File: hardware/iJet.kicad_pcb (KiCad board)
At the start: 2 copper layers, 82.3 x 116.7 mm, 107 parts, among them J1 GPIO, J12 Battery_Meas, J13 ICSP_Header_2, J14 5V_In, J15 Stat_LED, J16 ICSP_Header_1, J17 Button_Header, J18 RPI_POWER, J2 Status_LED_Header, J3 HP_LED_Header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

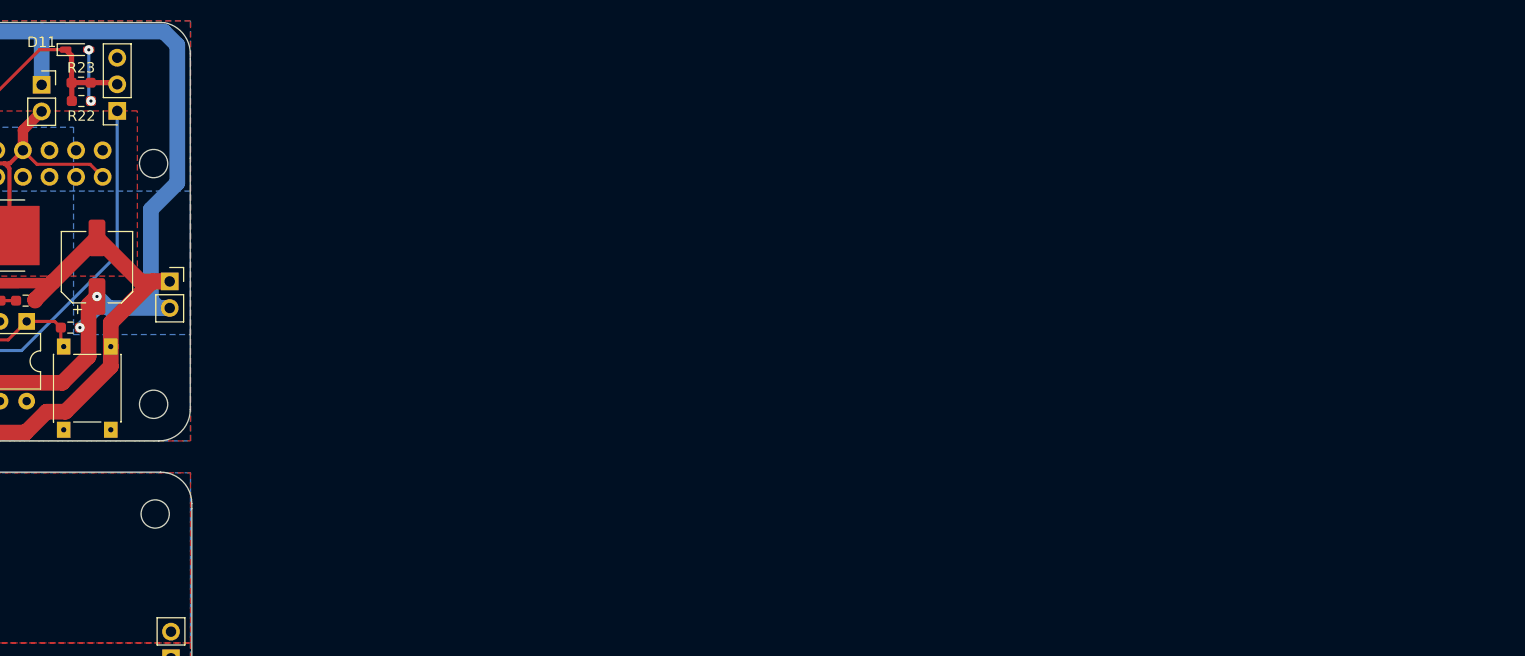
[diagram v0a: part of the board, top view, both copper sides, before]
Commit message: Hardware V0.2 - Schematics update
Combines Cell holder, BMS, and voltage regulator into single board
complete w. extensive electrical and thermal protections including:

* MM3220 BMS w Overvoltage, Overcurrent, undervoltage charging/discharge protect
* Fuses on cells, 12v in, 5v and 8.4v out.
* Reverse polarity protection on 12v and cells.

Adds debug UART header
Single IO header on every board
Minor component size corrections
Add current limiting resistor to RPI power NMOS gate.
Add optional support for MLCC/tantalum caps for Voltage Regulator instead of electrolytic
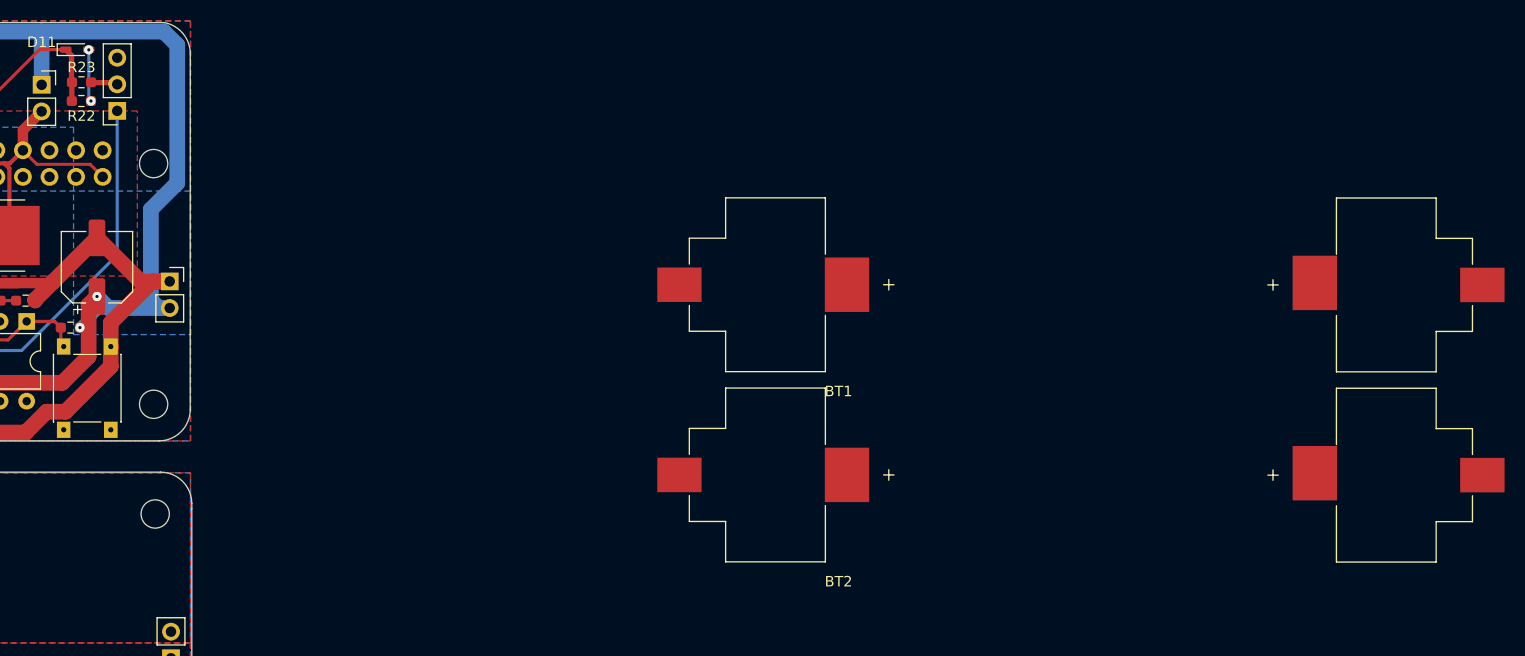
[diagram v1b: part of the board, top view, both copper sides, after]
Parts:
- added BT1: Battery_Cell, 254:BAT_254, F.Cu at (222.1, 85.1)
- added BT2: Battery_Cell, 254:BAT_254, F.Cu at (222.1, 103.3)
- moved R23 0.06 mm to (154.6, 65.7)
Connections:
- U4 pad 15: unconnected-(U4-PB1-Pad15) -> /Power State/LED_EN
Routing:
- net /Power State/Batt_Lvl: track 49.2 -> 47.4 mm
